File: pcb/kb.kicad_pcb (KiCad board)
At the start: 2 copper layers, 285.8 x 97.6 mm, 134 parts, among them J1 S2B-PH-SM4-TB, SW1 Gateron_LP_2.0, SW10 Gateron_LP_2.0, SW11 Gateron_LP_2.0, SW12 Gateron_LP_2.0, SW13 Gateron_LP_2.0, SW14 Gateron_LP_2.0, SW15 Gateron_LP_2.0, SW16 Gateron_LP_2.0, SW17 Gateron_LP_2.0, SW18 Gateron_LP_2.0, SW19 Gateron_LP_2.0, SW2 Gateron_LP_2.0, SW20 Gateron_LP_2.0, SW21 Gateron_LP_2.0, SW22 Gateron_LP_2.0, SW23 Gateron_LP_2.0, SW24 Gateron_LP_2.0, SW25 Gateron_LP_2.0, SW26 Gateron_LP_2.0, SW27 Gateron_LP_2.0, SW28 Gateron_LP_2.0, SW29 Gateron_LP_2.0, SW3 Gateron_LP_2.0, SW30 Gateron_LP_2.0, SW31 Gateron_LP_2.0, SW32 Gateron_LP_2.0, SW33 Gateron_LP_2.0, SW34 Gateron_LP_2.0, SW35 Gateron_LP_2.0, SW36 Gateron_LP_2.0, SW37 Gateron_LP_2.0, SW38 Gateron_LP_2.0, SW39 Gateron_LP_2.0, SW4 Gateron_LP_2.0, SW40 Gateron_LP_2.0, SW41 Gateron_LP_2.0, SW42 Gateron_LP_2.0, SW43 Gateron_LP_2.0, SW44 Gateron_LP_2.0, SW45 Gateron_LP_2.0, SW46 Gateron_LP_2.0, SW47 Gateron_LP_2.0, SW48 Gateron_LP_2.0, SW49 Gateron_LP_2.0, SW5 Gateron_LP_2.0, SW50 Gateron_LP_2.0, SW51 Gateron_LP_2.0, SW52 Gateron_LP_2.0, SW53 Gateron_LP_2.0, SW54 Gateron_LP_2.0, SW55 Gateron_LP_2.0, SW56 Gateron_LP_2.0, SW57 Gateron_LP_2.0, SW58 Gateron_LP_2.0, SW59 Gateron_LP_2.0, SW6 Gateron_LP_2.0, SW60 Gateron_LP_2.0, SW61 Gateron_LP_2.0, SW62 Gateron_LP_2.0, SW63 Gateron_LP_2.0, SW64 Gateron_LP_2.0, SW7 Gateron_LP_2.0, SW8 Gateron_LP_2.0, SW9 Gateron_LP_2.0, U1 SuperMini nRF52840

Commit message: battery switch
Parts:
- added SW0: SW_SPDT, Button_Switch_SMD:SW_SPDT_CK_JS102011SAQN, B.Cu at (33.3, 58.9)
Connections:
- J1 pad 2: GND -> Net-(J1-Pin_2)
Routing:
- net Net-(J1-Pin_2): track 0.00 -> 55.6 mm
- net GND: track 86.5 -> 38.8 mm

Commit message: finalize pcb
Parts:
- added REF**: MountingHole_5mm, MountingHole:MountingHole_5mm, F.Cu at (57.1, 57.1)
- added REF**: MountingHole_5mm, MountingHole:MountingHole_5mm, F.Cu at (54.8, 116.7)
- added REF**: MountingHole_5mm, MountingHole:MountingHole_5mm, F.Cu at (297.7, 112.1)
- added REF**: MountingHole_5mm, MountingHole:MountingHole_5mm, F.Cu at (164.3, 38.1)
- added REF**: MountingHole_3.2mm_M3, MountingHole:MountingHole_3.2mm_M3, F.Cu at (150.0, 116.7)
- added REF**: MountingHole_5mm, MountingHole:MountingHole_5mm, F.Cu at (290.5, 57.1)
- moved D63 0.29 mm to (295.3, 117.0)
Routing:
- net Net-(D54-A): track 16.3 -> 17.5 mm

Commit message: fix all known issues with v1.0 pcb
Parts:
- removed the REF** at (164.3, 38.1)
- moved D56 126.4 mm to (50.0, 116.7), turned to -90 degrees
- moved D57 102.4 mm to (73.8, 116.7), turned to -90 degrees
- moved D58 78.6 mm to (97.6, 116.7), turned to -90 degrees
- moved D59 50.5 mm to (169.1, 116.7)
- moved D43 22.5 mm to (85.7, 97.6), turned to -90 degrees
- moved D48 22.5 mm to (181.0, 97.6)
- moved D3 21.3 mm to (85.7, 40.5), turned to -90 degrees
- moved D6 21.3 mm to (142.9, 40.5), turned to -90 degrees
- moved D4 21.3 mm to (104.8, 40.5), turned to -90 degrees
- moved D5 21.3 mm to (123.8, 40.5), turned to -90 degrees
- moved D7 21.3 mm to (161.9, 40.5), turned to -90 degrees
- moved D2 20.5 mm to (64.3, 42.9), turned to 180 degrees
- moved D34 20.3 mm to (157.2, 77.8), turned to -90 degrees
- moved D31 20.3 mm to (100.0, 77.8), turned to -90 degrees
- moved D32 20.3 mm to (119.1, 77.8), turned to -90 degrees
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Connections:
- D1 pad 1: Net-(D1-K) -> /COL1
- D15 pad 1: Net-(D15-K) -> /COL1
- D15 pad 2: Net-(D1-K) -> Net-(D15-A)
- D16 pad 1: Net-(D16-K) -> /COL2
- D17 pad 1: Net-(D17-K) -> /COL3
- D18 pad 1: Net-(D18-K) -> /COL4
- D19 pad 1: Net-(D19-K) -> /COL5
- D2 pad 1: Net-(D16-A) -> /COL2
- D20 pad 1: Net-(D20-K) -> /COL6
- D21 pad 1: Net-(D21-K) -> /COL7
- D22 pad 1: Net-(D22-K) -> /COL7
- D23 pad 1: Net-(D23-K) -> /COL6
- D24 pad 1: Net-(D10-A) -> /COL5
- D25 pad 1: Net-(D11-A) -> /COL4
- D26 pad 1: Net-(D12-A) -> /COL3
- D27 pad 1: Net-(D13-A) -> /COL2
- D28 pad 1: Net-(D14-A) -> /COL1
- D29 pad 1: Net-(D29-K) -> /COL1
- D29 pad 2: Net-(D15-K) -> Net-(D29-A)
- D3 pad 1: Net-(D17-A) -> /COL3
- D30 pad 1: Net-(D30-K) -> /COL2
- D30 pad 2: Net-(D16-K) -> Net-(D30-A)
- D31 pad 1: Net-(D31-K) -> /COL3
- D31 pad 2: Net-(D17-K) -> Net-(D31-A)
- D32 pad 1: Net-(D32-K) -> /COL4
- D32 pad 2: Net-(D18-K) -> Net-(D32-A)
- D33 pad 1: Net-(D33-K) -> /COL5
- D33 pad 2: Net-(D19-K) -> Net-(D33-A)
- D34 pad 1: Net-(D34-K) -> /COL6
- D34 pad 2: Net-(D20-K) -> Net-(D34-A)
- D35 pad 1: Net-(D35-K) -> /COL7
- D35 pad 2: Net-(D21-K) -> Net-(D35-A)
- D36 pad 1: Net-(D22-A) -> /COL7
- D37 pad 1: Net-(D23-A) -> /COL6
- D38 pad 1: Net-(D24-A) -> /COL5
- D39 pad 1: Net-(D25-A) -> /COL4
- D4 pad 1: Net-(D18-A) -> /COL4
- D40 pad 1: Net-(D26-A) -> /COL3
- D41 pad 1: Net-(D27-A) -> /COL2
- D42 pad 1: Net-(D42-K) -> /COL1
- D42 pad 2: Net-(D29-K) -> Net-(D42-A)
- D43 pad 1: Net-(D43-K) -> /COL2
- D43 pad 2: Net-(D30-K) -> Net-(D43-A)
- D44 pad 1: Net-(D44-K) -> /COL3
- D44 pad 2: Net-(D31-K) -> Net-(D44-A)
- D45 pad 1: Net-(D45-K) -> /COL4
- D45 pad 2: Net-(D32-K) -> Net-(D45-A)
- D46 pad 1: Net-(D46-K) -> /COL5
- D46 pad 2: Net-(D33-K) -> Net-(D46-A)
- D47 pad 1: Net-(D47-K) -> /COL6
- D47 pad 2: Net-(D34-K) -> Net-(D47-A)
- D48 pad 1: Net-(D48-K) -> /COL7
- D48 pad 2: Net-(D35-K) -> Net-(D48-A)
- D49 pad 1: Net-(D36-A) -> /COL7
- D49 pad 2: Net-(D48-K) -> Net-(D49-A)
- D5 pad 1: Net-(D19-A) -> /COL5
- D50 pad 1: Net-(D37-A) -> /COL6
- D51 pad 1: Net-(D38-A) -> /COL5
- D52 pad 1: Net-(D39-A) -> /COL4
- D53 pad 1: Net-(D40-A) -> /COL3
- D54 pad 1: Net-(D41-A) -> /COL2
- D55 pad 1: Net-(D28-A) -> /COL1
- D56 pad 1: Net-(D56-K) -> /COL1
- D56 pad 2: Net-(D42-K) -> Net-(D56-A)
- D57 pad 1: Net-(D57-K) -> /COL2
- D57 pad 2: Net-(D43-K) -> Net-(D57-A)
- D58 pad 1: Net-(D58-K) -> /COL3
- D58 pad 2: Net-(D44-K) -> Net-(D58-A)
- D59 pad 1: Net-(D50-A) -> /COL6
- D59 pad 2: Net-(D47-K) -> Net-(D59-A)
- D6 pad 1: Net-(D20-A) -> /COL6
- D60 pad 1: Net-(D51-A) -> /COL5
- D60 pad 2: Net-(D46-K) -> Net-(D60-A)
- D61 pad 1: Net-(D52-A) -> /COL4
- D61 pad 2: Net-(D45-K) -> Net-(D61-A)
- D62 pad 1: Net-(D53-A) -> /COL3
- D62 pad 2: Net-(D58-K) -> Net-(D62-A)
- D63 pad 1: Net-(D54-A) -> /COL2
- D63 pad 2: Net-(D57-K) -> Net-(D63-A)
- D64 pad 1: Net-(D55-A) -> /COL1
- D64 pad 2: Net-(D56-K) -> Net-(D64-A)
- D7 pad 1: Net-(D21-A) -> /COL7
- D8 pad 2: Net-(D22-K) -> Net-(D8-A)
- D9 pad 2: Net-(D23-K) -> Net-(D9-A)
- SW0 pad 1: Net-(J1-Pin_2) -> Net-(J1-Pin_1)
- SW15 pad 2: Net-(D1-K) -> Net-(D15-A)
- SW29 pad 2: Net-(D15-K) -> Net-(D29-A)
- SW30 pad 2: Net-(D16-K) -> Net-(D30-A)
- SW31 pad 2: Net-(D17-K) -> Net-(D31-A)
- SW32 pad 2: Net-(D18-K) -> Net-(D32-A)
- SW33 pad 2: Net-(D19-K) -> Net-(D33-A)
- SW34 pad 2: Net-(D20-K) -> Net-(D34-A)
- SW35 pad 2: Net-(D21-K) -> Net-(D35-A)
- SW42 pad 2: Net-(D29-K) -> Net-(D42-A)
- SW43 pad 2: Net-(D30-K) -> Net-(D43-A)
- SW44 pad 2: Net-(D31-K) -> Net-(D44-A)
- SW45 pad 2: Net-(D32-K) -> Net-(D45-A)
- SW46 pad 2: Net-(D33-K) -> Net-(D46-A)
- SW47 pad 2: Net-(D34-K) -> Net-(D47-A)
- SW48 pad 2: Net-(D35-K) -> Net-(D48-A)
- SW49 pad 2: Net-(D48-K) -> Net-(D49-A)
- SW56 pad 2: Net-(D42-K) -> Net-(D56-A)
- SW57 pad 2: Net-(D43-K) -> Net-(D57-A)
- SW58 pad 2: Net-(D44-K) -> Net-(D58-A)
- SW59 pad 2: Net-(D47-K) -> Net-(D59-A)
- SW60 pad 2: Net-(D46-K) -> Net-(D60-A)
- SW61 pad 2: Net-(D45-K) -> Net-(D61-A)
- SW62 pad 2: Net-(D58-K) -> Net-(D62-A)
- SW63 pad 2: Net-(D57-K) -> Net-(D63-A)
- SW64 pad 2: Net-(D56-K) -> Net-(D64-A)
- SW8 pad 2: Net-(D22-K) -> Net-(D8-A)
- SW9 pad 2: Net-(D23-K) -> Net-(D9-A)
- U1 pad 13: Net-(J1-Pin_1) -> Net-(J1-Pin_2)
- U1 pad 29: Net-(J1-Pin_1) -> Net-(J1-Pin_2)
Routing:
- net /COL1: track 274.2 -> 711.7 mm
- net /COL2: track 232.0 -> 643.5 mm
- net /COL3: track 210.3 -> 569.0 mm
- net /COL4: track 188.5 -> 491.5 mm
- net /COL5: track 166.5 -> 440.5 mm
- net /COL6: track 147.2 -> 357.2 mm
- net Net-(D45-K): track 157.0 -> 0.00 mm
- net /COL7: track 123.3 -> 276.5 mm
- net Net-(D56-K): track 142.2 -> 0.00 mm
- net Net-(D42-K): track 131.9 -> 0.00 mm
- net Net-(D57-K): track 124.9 -> 0.00 mm
- net Net-(D46-K): track 121.5 -> 0.00 mm
- net Net-(D43-K): track 111.4 -> 0.00 mm
- net Net-(D58-K): track 107.5 -> 0.00 mm
- net Net-(D44-K): track 91.8 -> 0.00 mm
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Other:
- board text added: "- +"
- board text removed: "+ -"

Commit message: bump pcb version
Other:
- board text added: "KB60 V1.1"
- board text removed: "KB60 V1.0"
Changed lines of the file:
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@@
 		(layer "Edge.Cuts")
 	)
-	(gr_text "KB60 V1.0\n"
+	(gr_text "KB60 V1.1"
 		(at 171.45 117.39575 0)
 		(layer "F.SilkS")
@@
 			(justify left bottom)
 		)
-		(render_cache "KB60 V1.0\n" 0
+		(render_cache "KB60 V1.1" 0
 			(polygon
 				(pts
@@
 			(polygon
 				(pts
-					(xy 203.707575 113.985425) (xy 203.824328 114.052827) (xy 203.900797 114.160168) (xy 203.928192 114.313862)
-					(xy 203.900642 114.473849) (xy 203.824328 114.584788) (xy 203.707347 114.654295) (xy 203.550654 114.679035)
-					(xy 203.393722 114.654285) (xy 203.276705 114.584788) (xy 203.200391 114.473849) (xy 203.172841 114.313862)
-					(xy 203.200236 114.160168) (xy 203.276705 114.052827) (xy 203.393494 113.985435) (xy 203.550654 113.961328)
+					(xy 202.228445 116.63075) (xy 202.228445 116.114451) (xy 203.475091 116.114451) (xy 203.475091 112.525913)
+					(xy 202.228445 113.457669) (xy 202.228445 112.809204) (xy 203.267363 112.034893) (xy 204.041673 112.034893)
+					(xy 204.041673 116.114451) (xy 205.061357 116.114451) (xy 205.061357 116.63075)
 				)
 			)
-			(polygon
-				(pts
-					(xy 203.865486 111.997195) (xy 204.133644 112.068715) (xy 204.363405 112.18303) (xy 204.560995 112.340441)
-					(xy 204.721862 112.535533) (xy 204.837921 112.760523) (xy 204.910136 113.021217) (xy 204.935511 113.325503)
-					(xy 204.935511 115.34014) (xy 204.915518 115.608505) (xy 204.858113 115.844991) (xy 204.765426 116.054825)
-					(xy 204.636316 116.243132) (xy 204.476859 116.399612) (xy 204.284023 116.526885) (xy 204.070375 116.61751)
-					(xy 203.827747 116.673943) (xy 203.550654 116.693673) (xy 203.235655 116.66846) (xy 202.967401 116.59698)
-					(xy 202.737608 116.482747) (xy 202.540038 116.325476) (xy 202.379161 116.130252) (xy 202.263102 115.905167)
-					(xy 202.190893 115.644421) (xy 202.165522 115.34014) (xy 202.165522 113.325503) (xy 202.713145 113.325503)
-					(xy 202.713145 115.34014) (xy 202.740192 115.587068) (xy 202.81715 115.792896) (xy 202.942855 115.966623)
-					(xy 203.109801 116.099631) (xy 203.3092 116.180545) (xy 203.550654 116.208973) (xy 203.791916 116.180546)
-					(xy 203.991131 116.099635) (xy 204.157903 115.966623) (xy 204.283769 115.792876) (xy 204.360813 115.587049)
-					(xy 204.387888 115.34014) (xy 204.387888 113.325503) (xy 204.360819 113.078777) (xy 204.283781 112.873036)
-					(xy 204.157903 112.699295) (xy 203.99111 112.566119) (xy 203.791896 112.485123) (xy 203.550654 112.45667)
-					(xy 203.30922 112.485124) (xy 203.109821 112.566123) (xy 202.942855 112.699295) (xy 202.817138 112.873016)
-					(xy 202.740186 113.078758) (xy 202.713145 113.325503) (xy 202.165522 113.325503) (xy 202.190897 113.021217)
-					(xy 202.263111 112.760523) (xy 202.37917 112.535533) (xy 202.540038 112.340441) (xy 202.737625 112.183041)
-					(xy 202.967425 112.068726) (xy 203.235673 111.997199) (xy 203.550654 111.97197)
-				)
-			)

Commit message: update footprints + bom
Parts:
- SW0: footprint Button_Switch_SMD:SW_SPDT_CK_JS102011SAQN -> alpsalpine:SW_SSSS811101
- moved SW0 0.51 mm to (32.8, 58.9)
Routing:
- net GND: track 38.8 -> 40.5 mm
- net Net-(J1-Pin_1): track 56.5 -> 58.0 mm

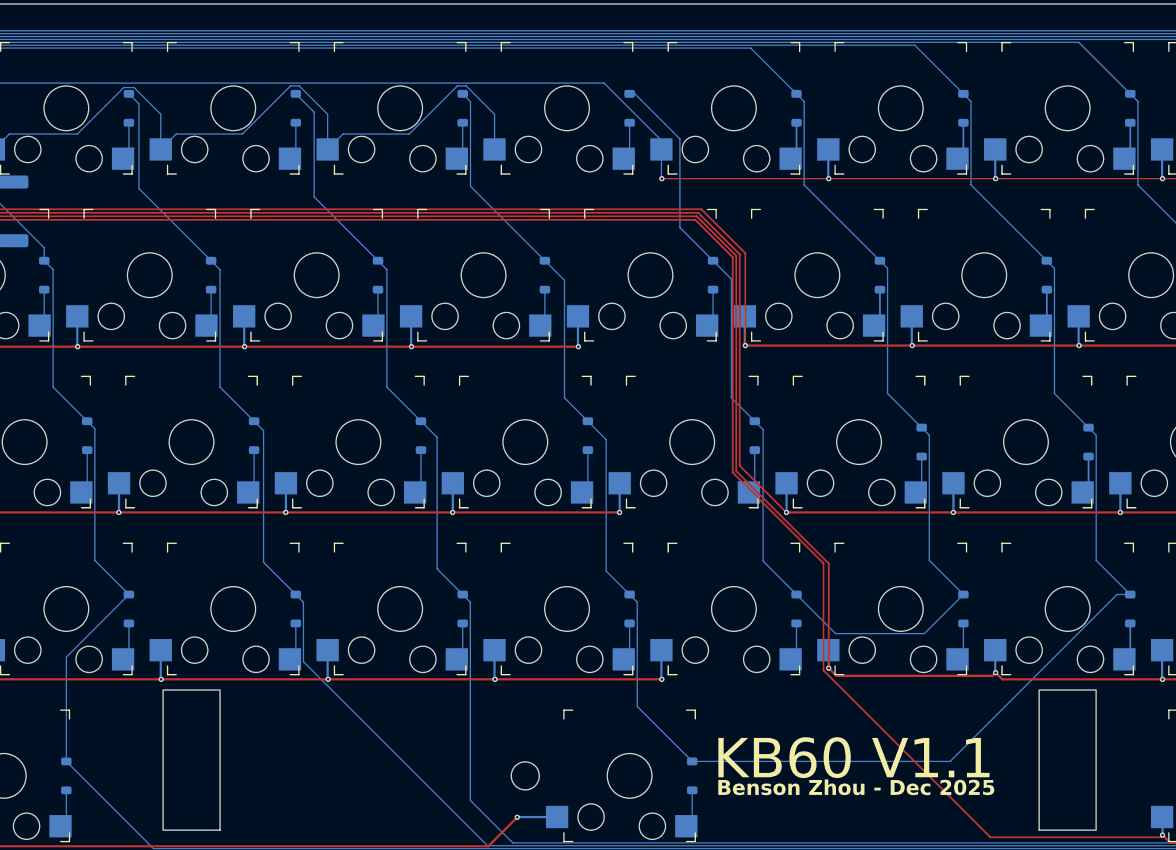
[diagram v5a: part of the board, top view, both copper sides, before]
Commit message: mounting holes
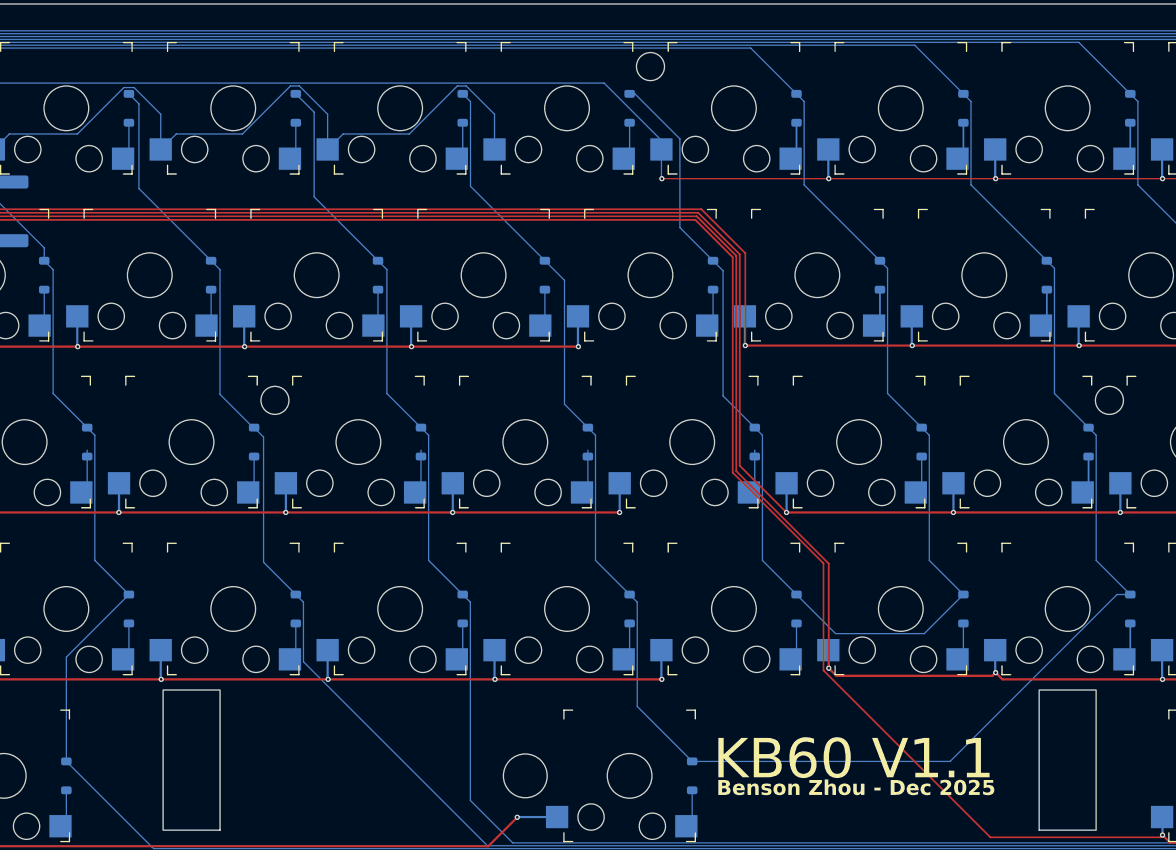
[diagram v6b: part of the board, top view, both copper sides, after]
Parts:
- added REF**: MountingHole_5mm, MountingHole:MountingHole_5mm, F.Cu at (150.0, 116.7)
- added REF**: MountingHole_3.2mm_M3, MountingHole:MountingHole_3.2mm_M3, F.Cu at (121.4, 73.8)
- added REF**: MountingHole_3.2mm_M3, MountingHole:MountingHole_3.2mm_M3, F.Cu at (216.7, 73.8)
- moved REF** 82.2 mm to (164.3, 35.7)
- moved D31 0.73 mm to (100.0, 78.6)
- moved D32 0.73 mm to (119.1, 78.6)
- moved D33 0.73 mm to (138.1, 78.6)
- moved D34 0.73 mm to (157.2, 78.6)
- moved D35 0.73 mm to (176.2, 78.6)
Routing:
- net Net-(D32-A): track 5.11 -> 4.38 mm
